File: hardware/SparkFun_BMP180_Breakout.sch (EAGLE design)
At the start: 16 parts, among them U1 BMP180

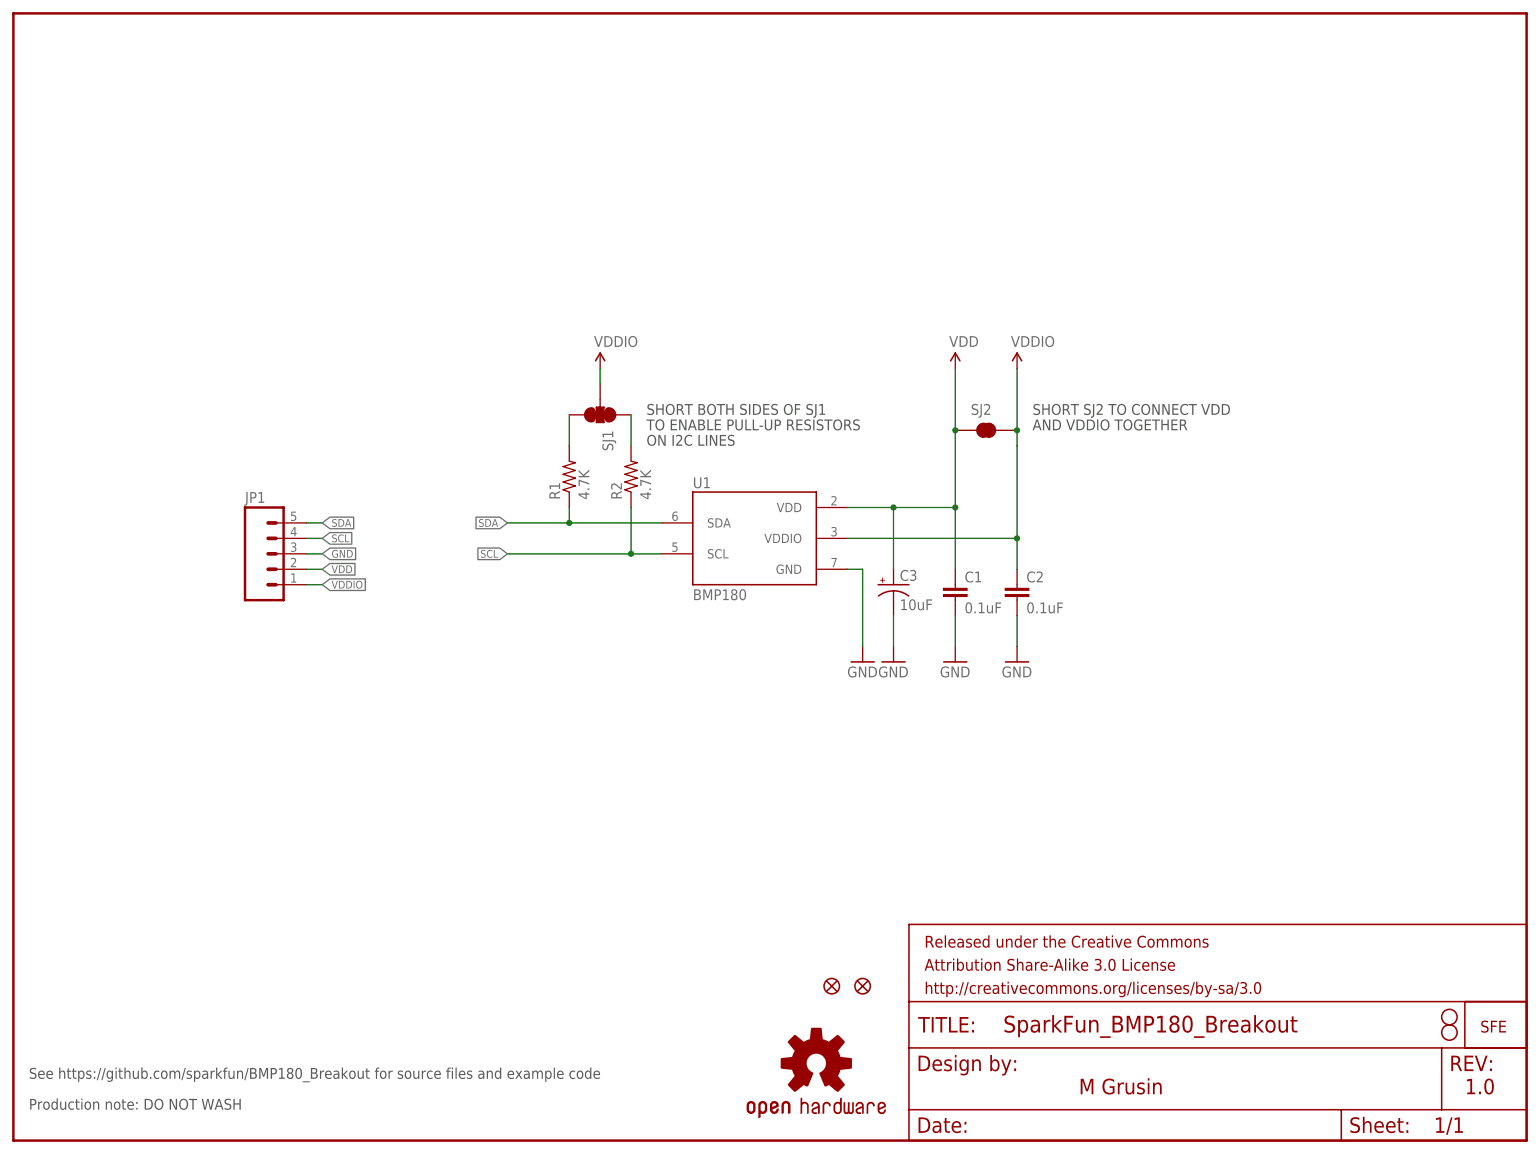
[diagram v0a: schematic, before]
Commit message: Version 2.0, initial commit
Rerouted connector for new standard I2C pinout.
Cleaned up layout and schematic per standards.
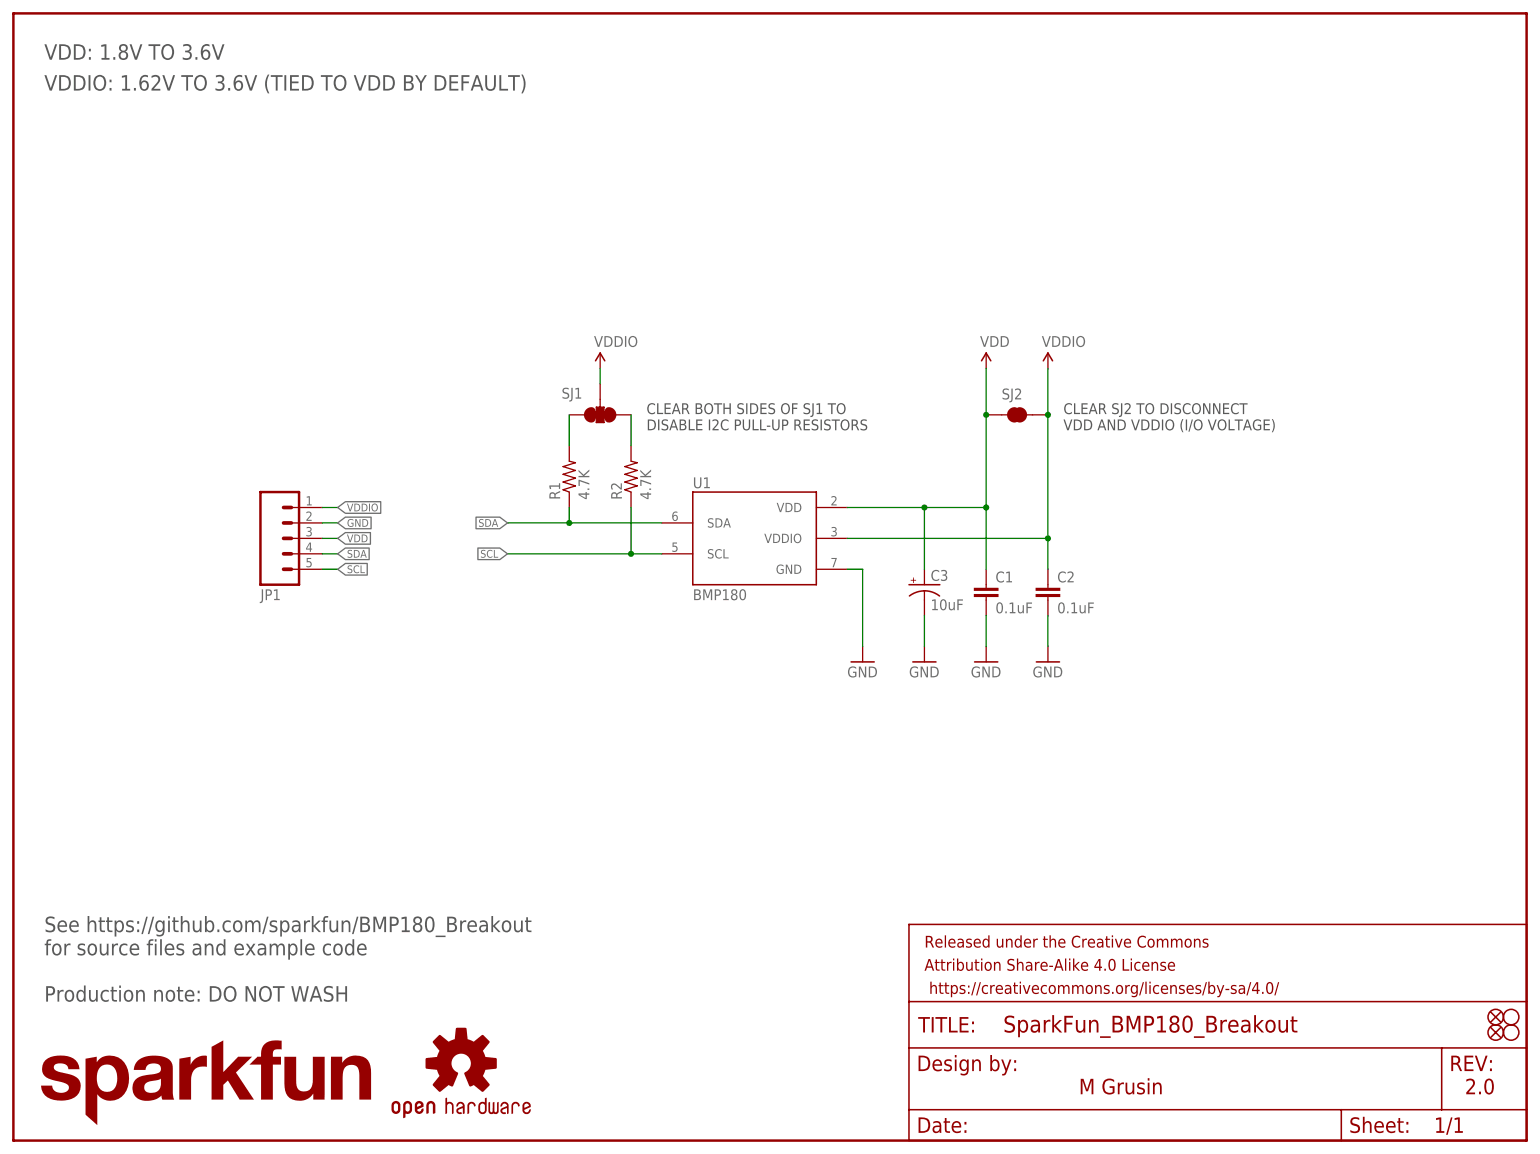
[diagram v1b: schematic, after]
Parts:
- removed LOGO1: LOGO-SFENW2, SparkFun-Aesthetics:LOGO-SFENW2
- added LOGO3: SFE_LOGO_NAME.1_INCH, SparkFun-Aesthetics:SFE_LOGO_NAME.1_INCH
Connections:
- net GND: now also JP1.2; no longer JP1.3
- net SCL: now also JP1.5; no longer JP1.4
- net SDA: now also JP1.4; no longer JP1.5
- net VDD: now also JP1.3; no longer JP1.2
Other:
- note added: "2.0"
- note added: "CLEAR BOTH SIDES OF SJ1 TO DISABLE I2C PULL-UP RESISTORS"
- note added: "CLEAR SJ2 TO DISCONNECT VDD AND VDDIO (I/O VOLTAGE)"
- note added: "VDD: 1.8V TO 3.6V"
- note added: "VDDIO: 1.62V TO 3.6V (TIED TO VDD BY DEFAULT)"
- note removed: "1.0"
- note removed: "AND VDDIO TOGETHER"
- note removed: "ON I2C LINES"
- note removed: "SHORT BOTH SIDES OF SJ1"
- note removed: "SHORT SJ2 TO CONNECT VDD"
- note removed: "TO ENABLE PULL-UP RESISTORS"
- moved on the sheet: C1, C2, C3, JP1, SJ2
